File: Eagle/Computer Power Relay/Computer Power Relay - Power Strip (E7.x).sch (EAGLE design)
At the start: 9 parts, among them K1 RELAY-3V3DC-110VAC012, K2 RELAY-110VACV3_IN-PLACE, K3 RELAY-110VACV3_SMD

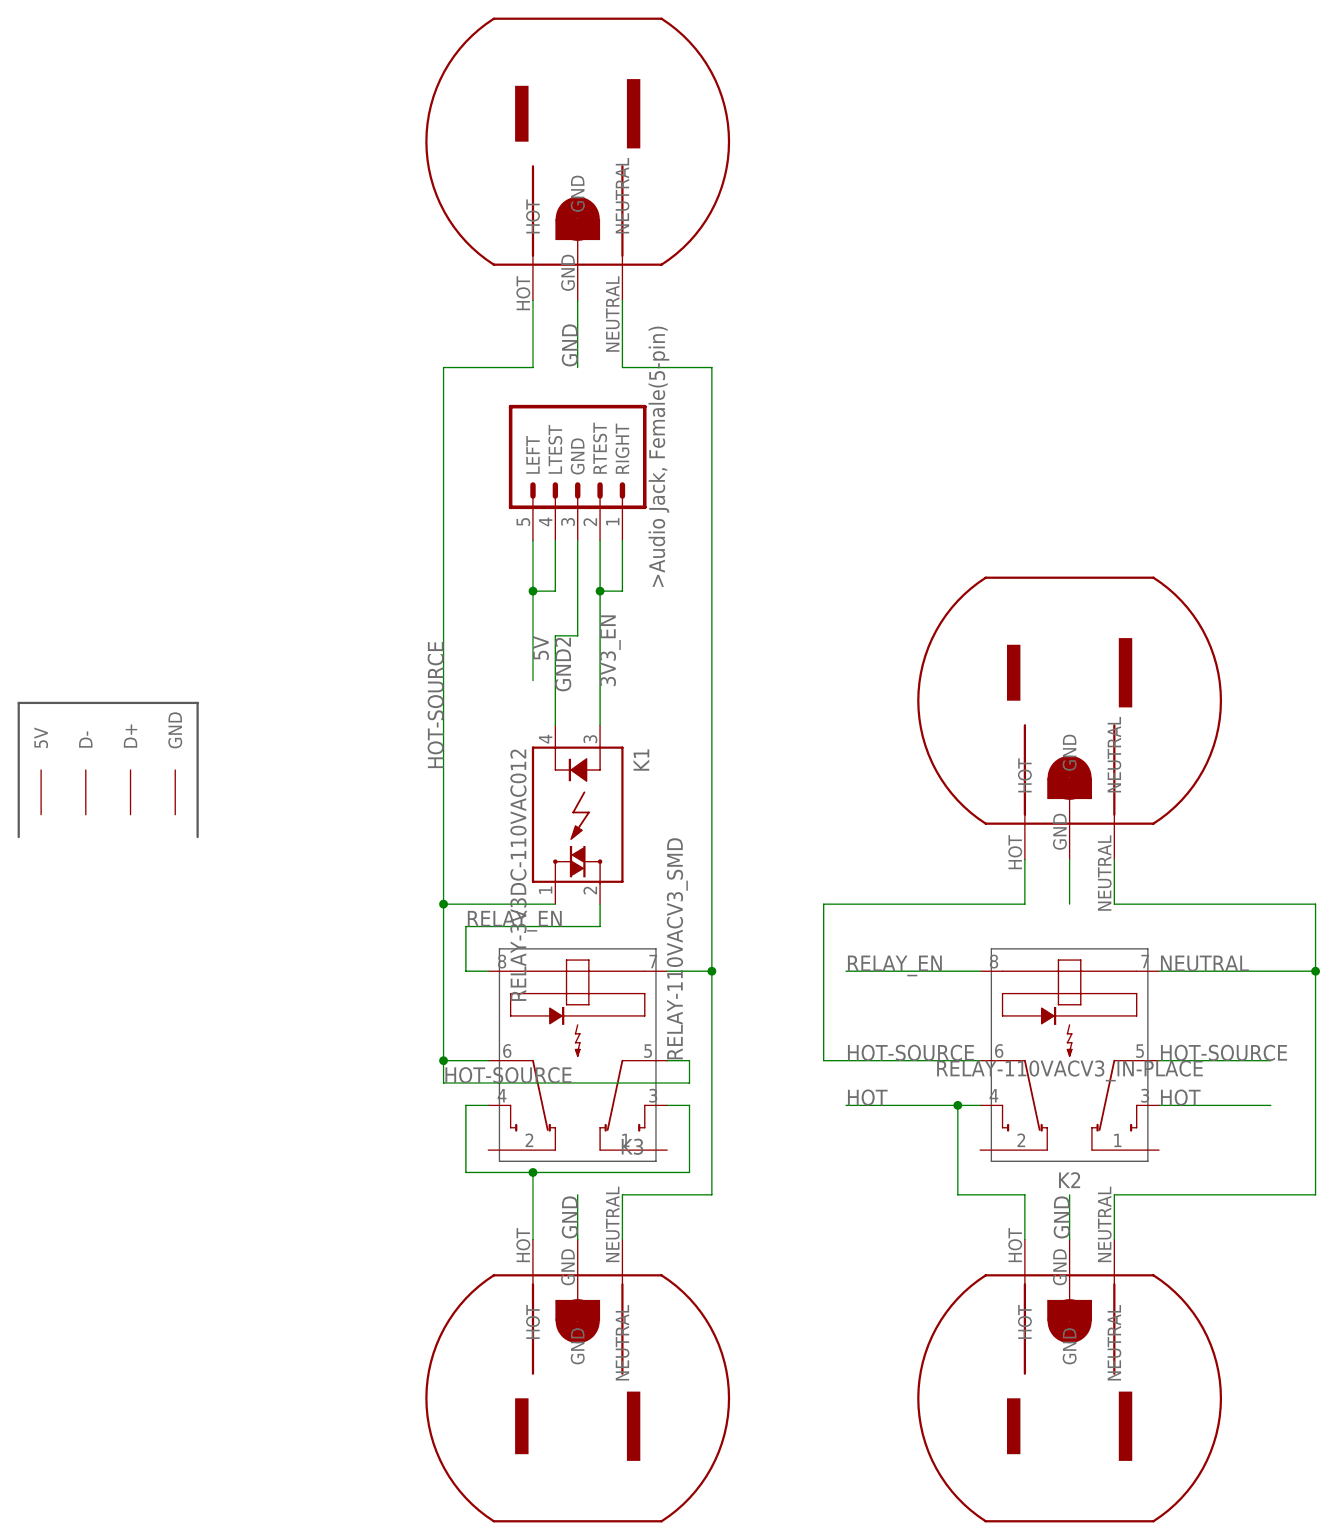
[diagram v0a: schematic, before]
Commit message: Beginning Merge of Boards (Relay)
I'm beginning to merge the Controller and Power Strip boards into one so that I can print it for cheaper.
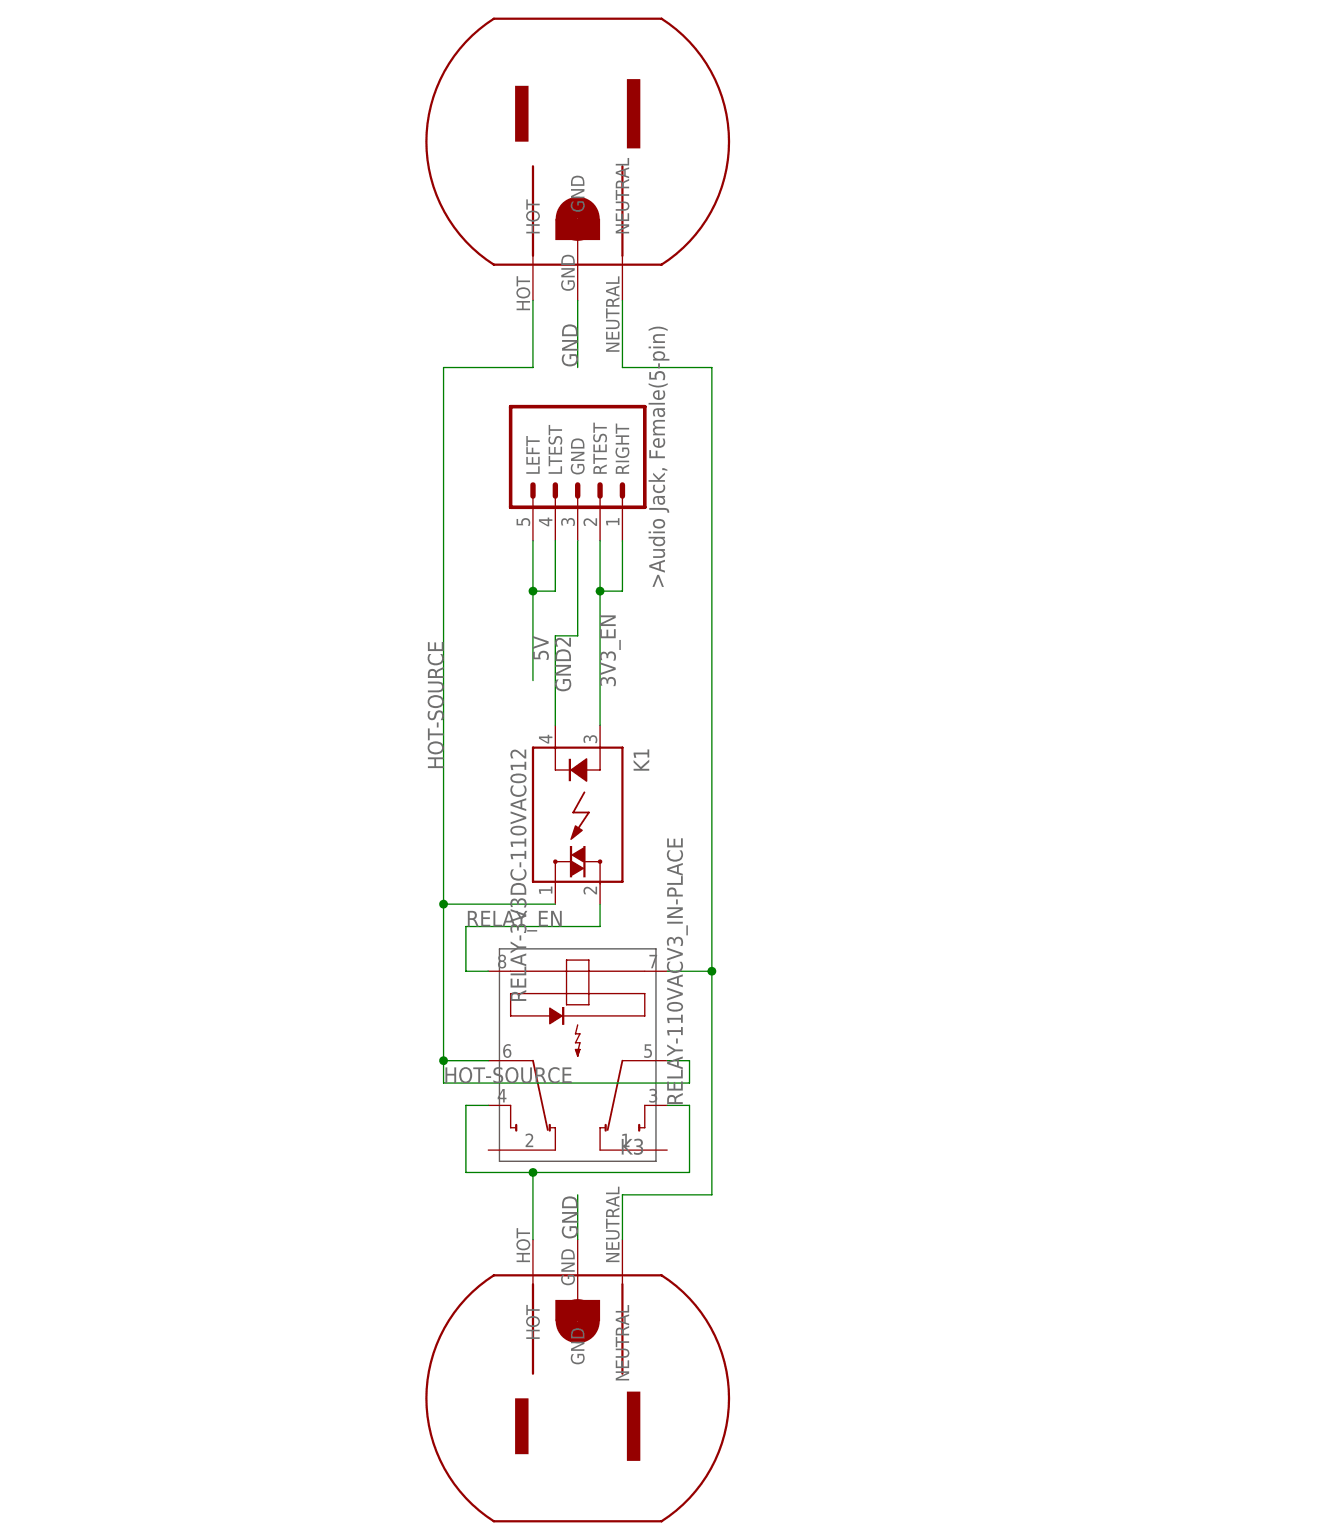
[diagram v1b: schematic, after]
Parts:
- removed K2: RELAY-110VACV3_IN-PLACE, Inventory:RELAY-110VACV3_IN-PLACE
- removed U$4, U$5: MAINS-POWER-OUTLET3-PIN, Inventory:MAINS-POWER-OUTLET3-PIN
- removed U$6: PCB_USB, Inventory:PCB_USB
- K3: value RELAY-110VACV3_SMD -> RELAY-110VACV3_IN-PLACE; device Inventory:RELAY-110VACV3_SMD -> Inventory:RELAY-110VACV3_IN-PLACE
- U$2, U$3: value MAINS-POWER-OUTLET3-PIN-SMD -> MAINS-POWER-OUTLET3-PIN; device Inventory:MAINS-POWER-OUTLET3-PIN-SMD -> Inventory:MAINS-POWER-OUTLET3-PIN
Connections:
- removed net HOT: K2.3, K2.4, U$4.HOT
- removed net N$3: U$5.GND
- removed net NEUTRAL: K2.7, U$4.NEUTRAL, U$5.NEUTRAL
- net GND: no longer U$4.GND
- net HOT-SOURCE: no longer K2.5, K2.6, U$5.HOT
- net RELAY_EN: no longer K2.8
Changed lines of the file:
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@@
 <?xml version="1.0" encoding="utf-8"?>
 <!DOCTYPE eagle SYSTEM "eagle.dtd">
-<eagle version="9.6.2">
+<eagle version="7.7.0">
 <drawing>
 <settings>
@@
 </classes>
 <parts>
-<part name="K3" library="Inventory" deviceset="RELAY-110VAC" device="V3_SMD" value="RELAY-110VACV3_SMD"/>
-<part name="K1" library="Inventory" deviceset="RELAY-3V3DC-110VAC" device="" package3d_urn="urn:adsk.eagle:package:24461/1" technology="012"/>
+<part name="K3" library="Inventory" deviceset="RELAY-110VAC" device="V3_IN-PLACE" value="RELAY-110VACV3_IN-PLACE"/>
+<part name="K1" library="Inventory" deviceset="RELAY-3V3DC-110VAC" device="" technology="012"/>
 <part name="U$1" library="Inventory" deviceset="AUDIO_JACK_FEMALE_5-PIN" device=""/>
-<part name="U$2" library="Inventory" deviceset="MAINS-POWER-OUTLET" device="3-PIN-SMD" value="MAINS-POWER-OUTLET3-PIN-SMD"/>
-<part name="U$3" library="Inventory" deviceset="MAINS-POWER-OUTLET" device="3-PIN-SMD" value="MAINS-POWER-OUTLET3-PIN-SMD"/>
-<part name="K2" library="Inventory" deviceset="RELAY-110VAC" device="V3_IN-PLACE"/>
-<part name="U$4" library="Inventory" deviceset="MAINS-POWER-OUTLET" device="3-PIN"/>
-<part name="U$5" library="Inventory" deviceset="MAINS-POWER-OUTLET" device="3-PIN"/>
-<part name="U$6" library="Inventory" deviceset="PCB_USB" device=""/>
+<part name="U$2" library="Inventory" deviceset="MAINS-POWER-OUTLET" device="3-PIN" value="MAINS-POWER-OUTLET3-PIN"/>
+<part name="U$3" library="Inventory" deviceset="MAINS-POWER-OUTLET" device="3-PIN" value="MAINS-POWER-OUTLET3-PIN"/>
 </parts>
 <sheets>
@@
 <instance part="U$2" gate="G$1" x="309.88" y="147.32" smashed="yes" rot="R180"/>
 <instance part="U$3" gate="G$1" x="309.88" y="284.48" smashed="yes" rot="MR0"/>
-<instance part="K2" gate="G$1" x="365.76" y="180.34" smashed="yes" rot="R180">
-<attribute name="NAME" x="365.76" y="170.18" size="1.778" layer="95" font="vector" rot="R180" align="bottom-center"/>
-<attribute name="VALUE" x="365.76" y="182.88" size="1.778" layer="96" font="vector" rot="R180" align="bottom-center"/>
-</instance>
-<instance part="U$4" gate="G$1" x="365.76" y="147.32" smashed="yes" rot="R180"/>
-<instance part="U$5" gate="G$1" x="365.76" y="220.98" smashed="yes" rot="MR0"/>
-<instance part="U$6" gate="A" x="256.54" y="208.28" smashed="yes"/>
 </instances>
 <busses>
@@
 <junction x="294.64" y="182.88"/>
 </segment>
-<segment>
-<pinref part="K2" gate="G$1" pin="6"/>
-<wire x1="355.6" y1="182.88" x2="337.82" y2="182.88" width="0.1524" layer="91"/>
-<label x="340.36" y="182.88" size="1.778" layer="95"/>
-<pinref part="U$5" gate="G$1" pin="HOT"/>
-<wire x1="360.68" y1="205.74" x2="360.68" y2="200.66" width="0.1524" layer="91"/>
-<wire x1="360.68" y1="200.66" x2="337.82" y2="200.66" width="0.1524" layer="91"/>
-<wire x1="337.82" y1="200.66" x2="337.82" y2="182.88" width="0.1524" layer="91"/>
-</segment>
-<segment>
-<pinref part="K2" gate="G$1" pin="5"/>
-<wire x1="375.92" y1="182.88" x2="388.62" y2="182.88" width="0.1524" layer="91"/>
-<label x="375.92" y="182.88" size="1.778" layer="95"/>
-</segment>
 </net>
 <net name="N$1" class="0">
@@
 <label x="297.18" y="198.12" size="1.778" layer="95"/>
 </segment>
-<segment>
-<pinref part="K2" gate="G$1" pin="8"/>
-<wire x1="355.6" y1="193.04" x2="340.36" y2="193.04" width="0.1524" layer="91"/>
-<label x="340.36" y="193.04" size="1.778" layer="95"/>
-</segment>
 </net>
 <net name="GND" class="0">
@@
 <wire x1="309.88" y1="269.24" x2="309.88" y2="261.62" width="0.1524" layer="91"/>
 <label x="309.88" y="261.62" size="1.778" layer="95" rot="R90"/>
-</segment>
-<segment>
-<pinref part="U$4" gate="G$1" pin="GND"/>
-<wire x1="365.76" y1="162.56" x2="365.76" y2="167.64" width="0.1524" layer="91"/>
-<label x="365.76" y="162.56" size="1.778" layer="95" rot="R90"/>
-</segment>
-</net>
-<net name="HOT" class="0">
-<segment>
-<pinref part="K2" gate="G$1" pin="4"/>
-<wire x1="355.6" y1="177.8" x2="353.06" y2="177.8" width="0.1524" layer="91"/>
-<label x="340.36" y="177.8" size="1.778" layer="95"/>
-<pinref part="U$4" gate="G$1" pin="HOT"/>
-<wire x1="353.06" y1="177.8" x2="340.36" y2="177.8" width="0.1524" layer="91"/>
-<wire x1="360.68" y1="162.56" x2="360.68" y2="167.64" width="0.1524" layer="91"/>
-<wire x1="360.68" y1="167.64" x2="353.06" y2="167.64" width="0.1524" layer="91"/>
-<wire x1="353.06" y1="167.64" x2="353.06" y2="177.8" width="0.1524" layer="91"/>
-<junction x="353.06" y="177.8"/>
-</segment>
-<segment>
-<pinref part="K2" gate="G$1" pin="3"/>
-<wire x1="375.92" y1="177.8" x2="388.62" y2="177.8" width="0.1524" layer="91"/>
-<label x="375.92" y="177.8" size="1.778" layer="95"/>
-</segment>
-</net>
-<net name="NEUTRAL" class="0">
-<segment>
-<pinref part="K2" gate="G$1" pin="7"/>
-<wire x1="375.92" y1="193.04" x2="393.7" y2="193.04" width="0.1524" layer="91"/>
-<label x="375.92" y="193.04" size="1.778" layer="95"/>
-<pinref part="U$4" gate="G$1" pin="NEUTRAL"/>
-<wire x1="370.84" y1="162.56" x2="370.84" y2="167.64" width="0.1524" layer="91"/>
-<wire x1="370.84" y1="167.64" x2="393.7" y2="167.64" width="0.1524" layer="91"/>
-<wire x1="393.7" y1="167.64" x2="393.7" y2="193.04" width="0.1524" layer="91"/>
-<pinref part="U$5" gate="G$1" pin="NEUTRAL"/>
-<wire x1="370.84" y1="205.74" x2="370.84" y2="200.66" width="0.1524" layer="91"/>
-<wire x1="370.84" y1="200.66" x2="393.7" y2="200.66" width="0.1524" layer="91"/>
-<wire x1="393.7" y1="200.66" x2="393.7" y2="193.04" width="0.1524" layer="91"/>
-<junction x="393.7" y="193.04"/>
-</segment>
-</net>
-<net name="N$3" class="0">
-<segment>
-<pinref part="U$5" gate="G$1" pin="GND"/>
-<wire x1="365.76" y1="205.74" x2="365.76" y2="200.66" width="0.1524" layer="91"/>
 </segment>
 </net>
@@
 which will not be processed correctly with this version.
 </note>
-<note version="8.3" severity="warning">
-Since Version 8.3, EAGLE supports URNs for individual library
-assets (packages, symbols, and devices). The URNs of those assets
-will not be understood (or retained) with this version.
-</note>
-<note version="8.3" severity="warning">
-Since Version 8.3, EAGLE supports the association of 3D packages
-with devices in libraries, schematics, and board files. Those 3D
-packages will not be understood (or retained) with this version.
-</note>
 </compatibility>
